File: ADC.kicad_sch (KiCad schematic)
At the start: 31 parts, among them J4 ANALOG VOLTAGE INPUTS, J5 DIFFERENTIAL INPUT, J6 CURRENT INPUTS, U5 REF3333, U6 ADS1261

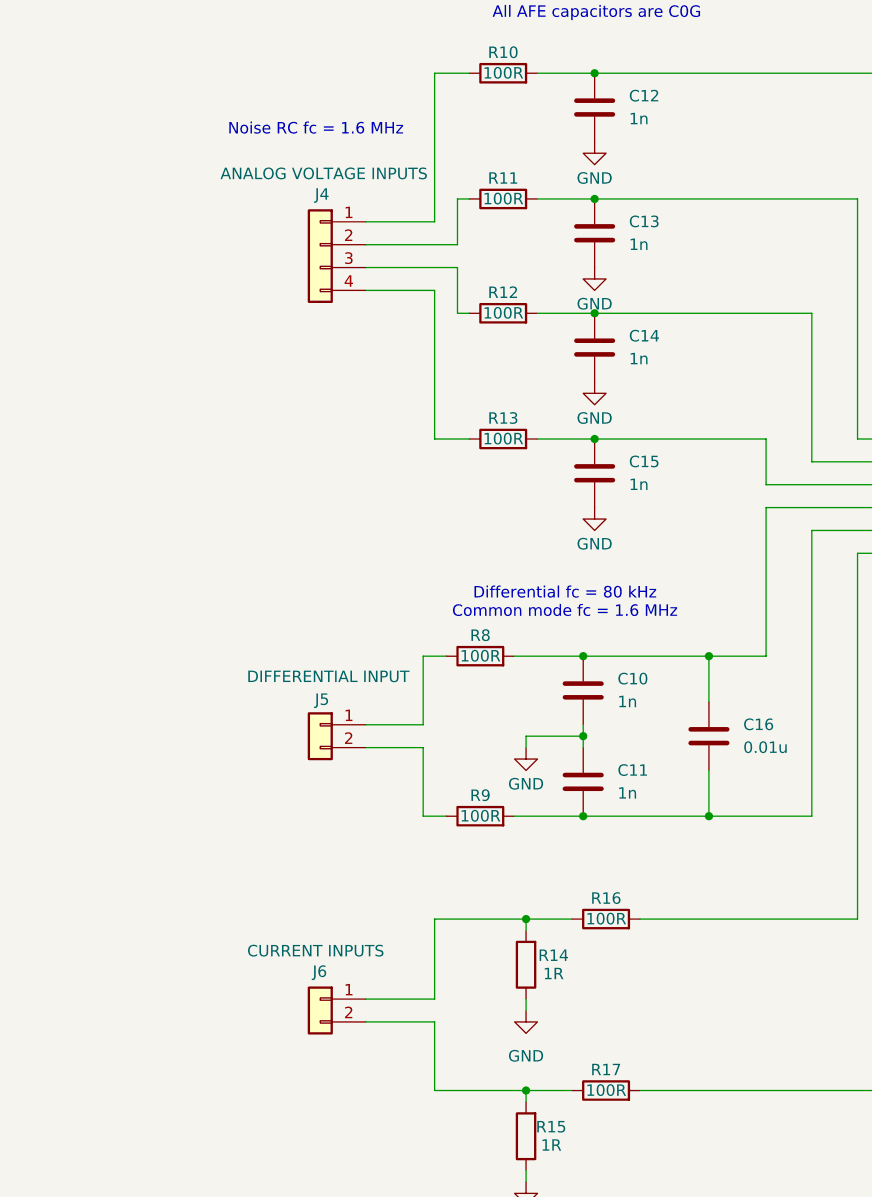
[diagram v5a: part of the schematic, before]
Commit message: Add screw terminals
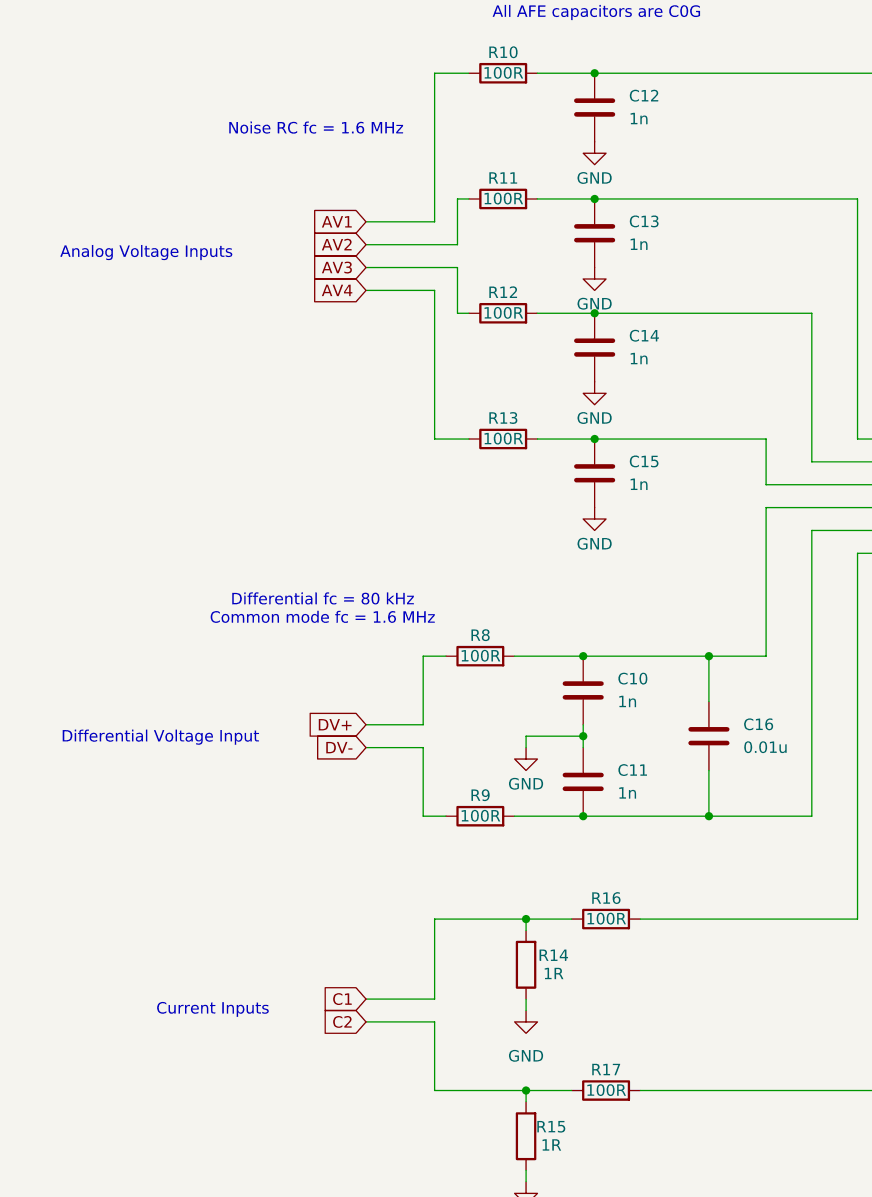
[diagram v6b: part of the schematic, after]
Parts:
- removed J4: ANALOG VOLTAGE INPUTS, symbol Connector_Generic:Conn_01x04
- removed J5: DIFFERENTIAL INPUT, symbol Connector_Generic:Conn_01x02
- removed J6: CURRENT INPUTS, symbol Connector_Generic:Conn_01x02
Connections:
- net C2: now reaches R15.2, R17.1
- net AV2: now reaches R11.1
- net AV1: now reaches R10.1
- net DV+: now reaches R8.1
- net DV-: now reaches R9.1
- net AV4: now reaches R13.1
- net C1: now reaches R14.2, R16.1
- net AV3: now reaches R12.1
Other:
- note added: "Analog Voltage Inputs"
- note added: "Current Inputs"
- note added: "Differential Voltage Input"

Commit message: Add 3D models and rearrange pins
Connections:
- net AV1: now also R13.1; no longer R10.1
- net AV2: now also R12.1; no longer R11.1
- net AV3: now also R11.1; no longer R12.1
- net AV4: now also R10.1; no longer R13.1
- net DV+: now also R9.1; no longer R8.1
- net DV-: now also R8.1; no longer R9.1
- net C1 renamed AC2
- net C2 renamed AC1
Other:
- note added: "AC1"
- note added: "AC2"
- note added: "AV1"
- note added: "AV2"
- note added: "AV3"
- note added: "AV4"
- note added: "Analog Current Inputs"
- note added: "DV+"
- note added: "DV-"
- note removed: "Analog 1"
- note removed: "Analog 2"
- note removed: "Analog 3"
- note removed: "Analog 4"
- note removed: "Current 1"
- note removed: "Current 2"
- note removed: "Current Inputs"
- note removed: "Diff. Analog +"
- note removed: "Diff. Analog -"
